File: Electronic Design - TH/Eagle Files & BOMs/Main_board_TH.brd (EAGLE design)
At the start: 90 x 137.2 mm, 41 parts, among them M1 ARDUINO-NANO-3.0, Q1 IRF9520, Q2 IRF9520

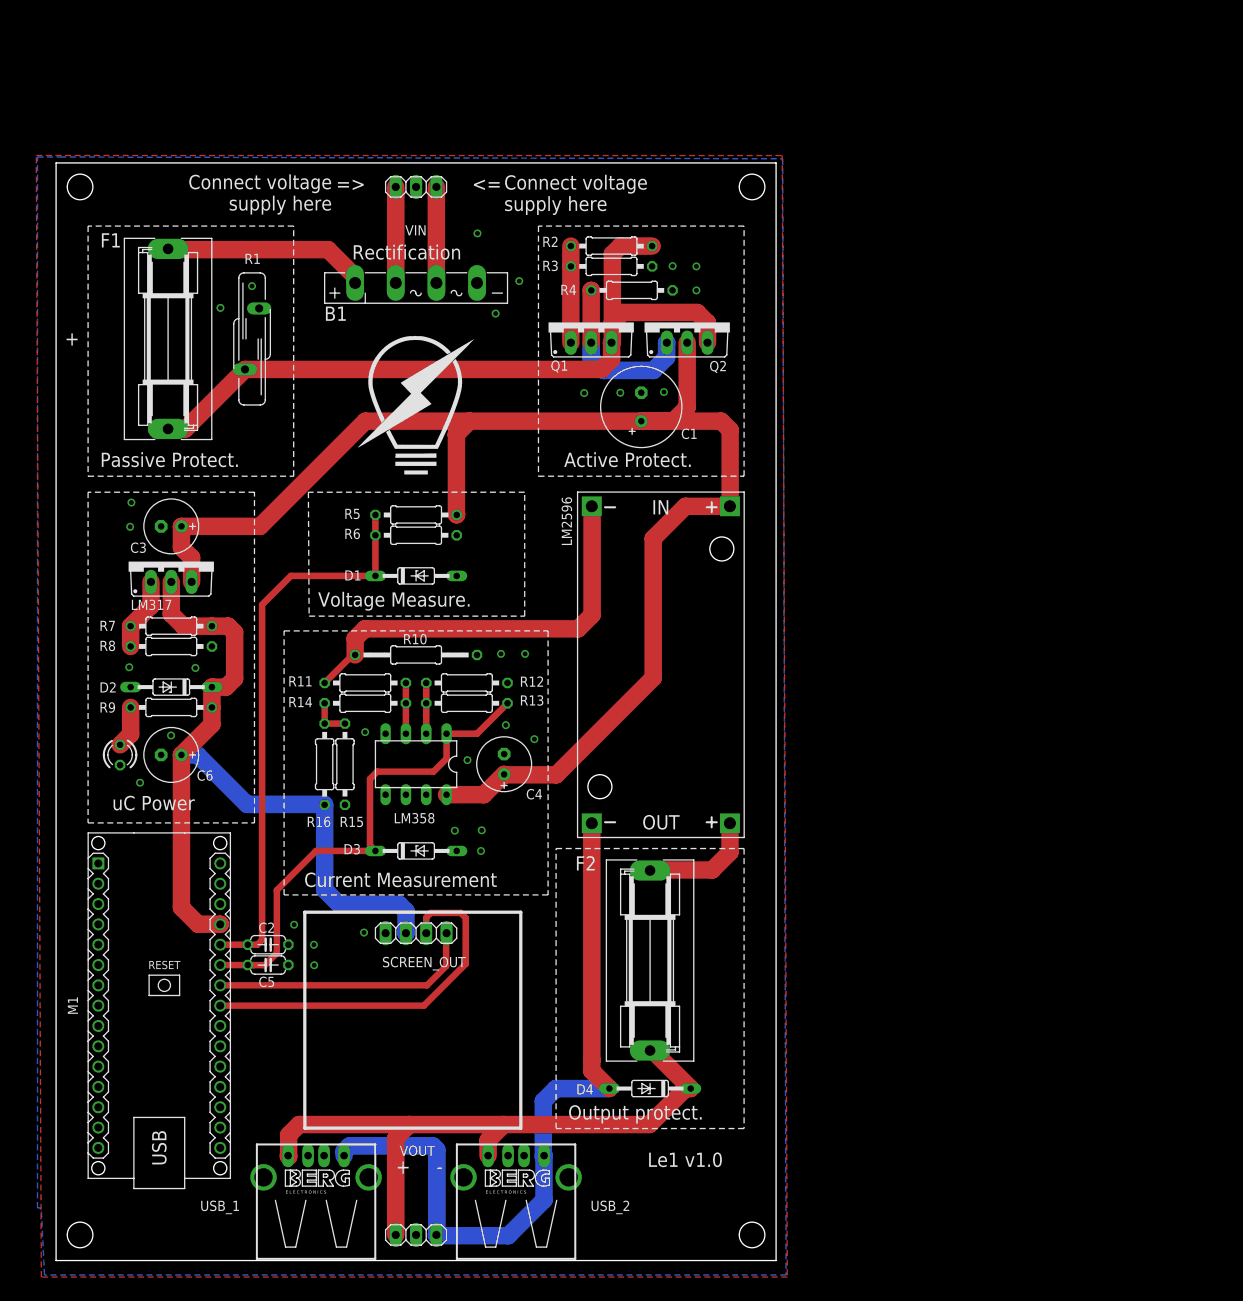
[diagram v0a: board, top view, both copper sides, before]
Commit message: reducing board size by 0.2mm to get it bang on 137mm
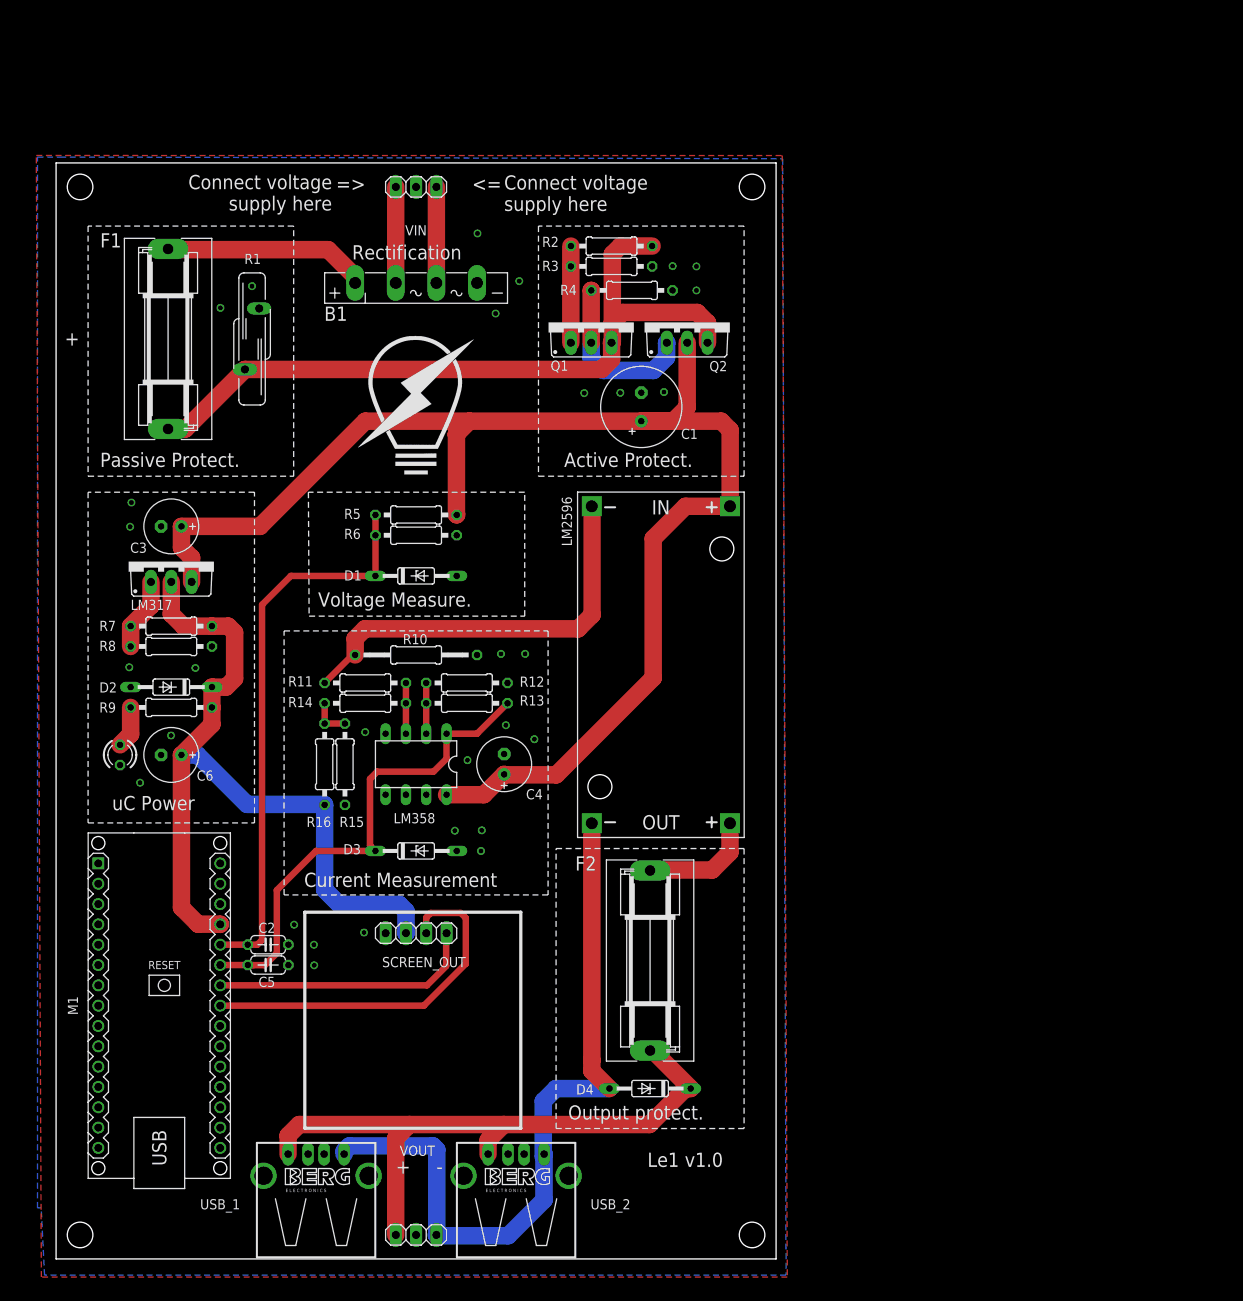
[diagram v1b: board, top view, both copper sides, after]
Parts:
- moved USB_1 0.20 mm to (32.5, 10.4)
- moved USB_2 0.20 mm to (57.5, 10.4)
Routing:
- net VOUT_FINAL: track 81.8 -> 81.1 mm
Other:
- board size 90 x 137.2 mm -> 90 x 137 mm
- board text removed: "C:/Users/kk/Downloads/path4501.bmp"
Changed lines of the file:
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@@
 <board>
 <plain>
-<wire x1="0" y1="137" x2="0" y2="-0.2" width="0" layer="20"/>
-<wire x1="0" y1="-0.2" x2="90" y2="-0.2" width="0" layer="20"/>
+<wire x1="0" y1="137" x2="0" y2="0" width="0" layer="20"/>
+<wire x1="0" y1="0" x2="90" y2="0" width="0" layer="20"/>
 <hole x="87" y="134" drill="3.2"/>
 <hole x="87" y="3" drill="3.2"/>
@@
 <hole x="3" y="134" drill="3.2"/>
 <wire x1="0" y1="137" x2="90" y2="137" width="0" layer="20"/>
-<wire x1="90" y1="-0.2" x2="90" y2="137" width="0" layer="20"/>
+<wire x1="90" y1="0" x2="90" y2="137" width="0" layer="20"/>
 <text x="2.92" y="115.95" size="1.778" layer="25" rot="R180">+</text>
 <wire x1="86" y1="129.11" x2="60.3" y2="129.11" width="0.15" layer="21" style="shortdash"/>
@@
 <rectangle x1="44.1071" y1="115.3287" x2="45.7073" y2="115.3541" layer="21"/>
 <rectangle x1="44.8183" y1="115.3541" x2="45.0215" y2="115.3795" layer="21"/>
-<text x="0" y="-0.127" size="0.0508" layer="200" font="vector">C:/Users/kk/Downloads/path4501.bmp</text>
 <rectangle x1="25" y1="22" x2="65" y2="30" layer="22"/>
 <text x="58.674" y="32.131" size="1.778" layer="22" rot="MR0">This Le1 belongs to:</text>
@@
 <attribute name="VALUE" x="71.6906" y="124.705" size="1.27" layer="27" ratio="10" rot="R180"/>
 </element>
-<element name="USB_1" library="con-berg" package="PN87520-S" value="PN87520-S" x="32.5" y="10.2" smashed="yes">
-<attribute name="MPN" value="" x="32.5" y="10.2" size="1.778" layer="27" display="off"/>
-<attribute name="OC_FARNELL" value="unknown" x="32.5" y="10.2" size="1.778" layer="27" display="off"/>
-<attribute name="OC_NEWARK" value="unknown" x="32.5" y="10.2" size="1.778" layer="27" display="off"/>
-<attribute name="MF" value="" x="32.5" y="10.2" size="1.778" layer="27" display="off"/>
-<attribute name="NAME" x="18" y="6" size="1.27" layer="25"/>
-<attribute name="VALUE" x="41.644" y="0.04" size="1.27" layer="27" rot="R90"/>
-</element>
-<element name="USB_2" library="con-berg" package="PN87520-S" value="PN87520-S" x="57.5" y="10.2" smashed="yes">
-<attribute name="MPN" value="" x="57.5" y="10.2" size="1.778" layer="27" display="off"/>
-<attribute name="OC_FARNELL" value="unknown" x="57.5" y="10.2" size="1.778" layer="27" display="off"/>
-<attribute name="OC_NEWARK" value="unknown" x="57.5" y="10.2" size="1.778" layer="27" display="off"/>
-<attribute name="MF" value="" x="57.5" y="10.2" size="1.778" layer="27" display="off"/>
-<attribute name="NAME" x="66.8" y="6" size="1.27" layer="25"/>
-<attribute name="VALUE" x="66.644" y="0.04" size="1.27" layer="27" rot="R90"/>
+<element name="USB_1" library="con-berg" package="PN87520-S" value="PN87520-S" x="32.5" y="10.4" smashed="yes">
+<attribute name="MPN" value="" x="32.5" y="10.4" size="1.778" layer="27" display="off"/>
+<attribute name="OC_FARNELL" value="unknown" x="32.5" y="10.4" size="1.778" layer="27" display="off"/>
+<attribute name="OC_NEWARK" value="unknown" x="32.5" y="10.4" size="1.778" layer="27" display="off"/>
+<attribute name="MF" value="" x="32.5" y="10.4" size="1.778" layer="27" display="off"/>
+<attribute name="NAME" x="18" y="6.2" size="1.27" layer="25"/>
+<attribute name="VALUE" x="41.644" y="0.24" size="1.27" layer="27" rot="R90"/>
+</element>
+<element name="USB_2" library="con-berg" package="PN87520-S" value="PN87520-S" x="57.5" y="10.4" smashed="yes">
+<attribute name="MPN" value="" x="57.5" y="10.4" size="1.778" layer="27" display="off"/>
+<attribute name="OC_FARNELL" value="unknown" x="57.5" y="10.4" size="1.778" layer="27" display="off"/>
+<attribute name="OC_NEWARK" value="unknown" x="57.5" y="10.4" size="1.778" layer="27" display="off"/>
+<attribute name="MF" value="" x="57.5" y="10.4" size="1.778" layer="27" display="off"/>
+<attribute name="NAME" x="66.8" y="6.2" size="1.27" layer="25"/>
+<attribute name="VALUE" x="66.644" y="0.24" size="1.27" layer="27" rot="R90"/>
 </element>
 </elements>
@@
 <contactref element="USB_2" pad="1"/>
 <wire x1="44.17" y1="16.8" x2="55.97" y2="16.8" width="2.1844" layer="1"/>
-<wire x1="44.17" y1="16.8" x2="30.38" y2="16.8" width="2.1844" layer="1"/>
-<wire x1="30.38" y1="16.8" x2="29.08" y2="15.5" width="2.1844" layer="1"/>
-<wire x1="29.08" y1="15.5" x2="29.08" y2="12.79" width="2.1844" layer="1"/>
-<wire x1="29.08" y1="12.79" x2="29" y2="12.91" width="2.1844" layer="1"/>
-<wire x1="54" y1="12.91" x2="54" y2="14.83" width="2.1844" layer="1"/>
+<wire x1="30.38" y1="16.8" x2="44.17" y2="16.8" width="2.1844" layer="1"/>
+<wire x1="54" y1="13.11" x2="54" y2="14.83" width="2.1844" layer="1"/>
 <wire x1="54" y1="14.83" x2="55.97" y2="16.8" width="2.1844" layer="1"/>
 <wire x1="42.46" y1="3" x2="42.46" y2="15.09" width="2.1844" layer="1"/>
@@
 <wire x1="79.33" y1="21.3" x2="78.68" y2="21.3" width="2.1844" layer="1"/>
 <wire x1="78.68" y1="21.3" x2="74.18" y2="16.8" width="2.1844" layer="1"/>
+<wire x1="29" y1="13.11" x2="29" y2="15.42" width="2.1844" layer="1"/>
+<wire x1="29" y1="15.42" x2="30.38" y2="16.8" width="2.1844" layer="1"/>
 </signal>
 <signal name="VOUT_PREFUSE">
@@
 <contactref element="USB_1" pad="4"/>
 <contactref element="USB_2" pad="4"/>
-<wire x1="36" y1="12.91" x2="36" y2="13.46" width="2.1844" layer="16"/>
+<wire x1="36" y1="13.11" x2="36" y2="13.46" width="2.1844" layer="16"/>
 <wire x1="36" y1="13.46" x2="36.67" y2="14.13" width="2.1844" layer="16"/>
 <wire x1="36.67" y1="14.13" x2="47.11" y2="14.13" width="2.1844" layer="16"/>
@@
 <wire x1="62.48" y1="21.3" x2="60.9" y2="19.72" width="2.1844" layer="16"/>
 <wire x1="60.9" y1="19.72" x2="60.9" y2="12.81" width="2.1844" layer="16"/>
-<wire x1="60.9" y1="12.81" x2="61" y2="12.91" width="2.1844" layer="16"/>
-<wire x1="61" y1="12.91" x2="61" y2="7.38" width="2.1844" layer="16"/>
+<wire x1="60.9" y1="12.81" x2="61" y2="13.11" width="2.1844" layer="16"/>
+<wire x1="61" y1="13.11" x2="61" y2="7.38" width="2.1844" layer="16"/>
 <wire x1="61" y1="7.38" x2="56.52" y2="2.9" width="2.1844" layer="16"/>
 <wire x1="56.52" y1="2.9" x2="47.64" y2="2.9" width="2.1844" layer="16"/>

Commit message: updating values of divider on Q1
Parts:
- R2: value 10k -> 13k
- R3: value 10k -> 100k
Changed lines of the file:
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@@
 <attribute name="VALUE" x="24.341" y="34.073" size="1.27" layer="27" ratio="10"/>
 </element>
-<element name="R2" library="resistor" package="0207/10" value="10k" x="69.43" y="126.61" smashed="yes">
+<element name="R2" library="resistor" package="0207/10" value="13k" x="69.43" y="126.61" smashed="yes">
 <attribute name="NAME" x="60.75" y="126.5" size="1.27" layer="25" ratio="10"/>
 <attribute name="VALUE" x="67.1694" y="125.975" size="1.27" layer="27" ratio="10"/>
 </element>
-<element name="R3" library="resistor" package="0207/10" value="10k" x="69.43" y="124.07" smashed="yes" rot="R180">
+<element name="R3" library="resistor" package="0207/10" value="100k" x="69.43" y="124.07" smashed="yes" rot="R180">
 <attribute name="NAME" x="60.75" y="123.5" size="1.27" layer="25" ratio="10"/>
 <attribute name="VALUE" x="71.6906" y="124.705" size="1.27" layer="27" ratio="10" rot="R180"/>
